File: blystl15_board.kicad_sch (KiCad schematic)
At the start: 3 parts, among them M1 BLYST NANO/L15

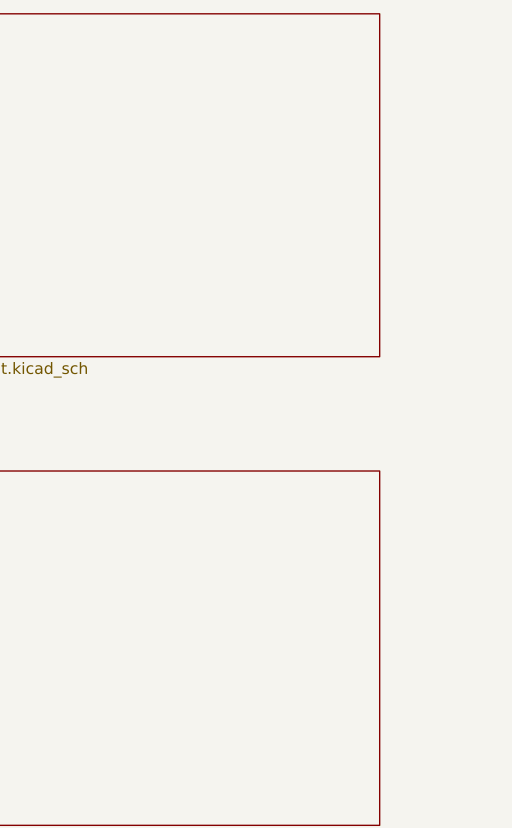
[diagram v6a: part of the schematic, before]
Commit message: PCB traces started
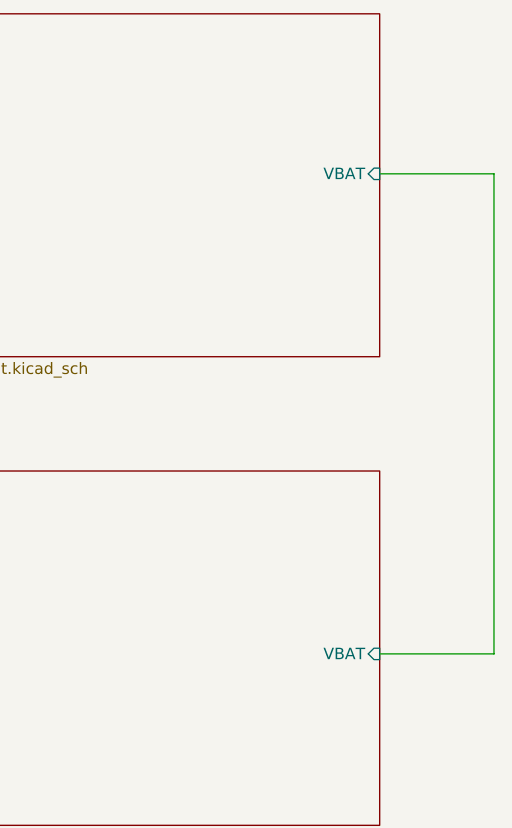
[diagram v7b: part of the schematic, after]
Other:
- sheet Power Management ports: added VBAT; removed none
- sheet Sensors ports: added VBAT; removed none
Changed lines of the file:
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@@
+	(wire
+		(pts
+			(xy 241.3 40.64) (xy 254 40.64)
+		)
+		(stroke
+			(width 0)
+			(type default)
+		)
+	)
 	(wire
 		(pts
@@
 	(wire
 		(pts
+			(xy 254 40.64) (xy 254 93.98)
+		)
+		(stroke
+			(width 0)
+			(type default)
+		)
+	)
+	(wire
+		(pts
 			(xy 158.75 138.43) (xy 177.8 138.43)
 		)
@@
 		(pts
 			(xy 158.75 100.33) (xy 177.8 100.33)
+		)
+		(stroke
+			(width 0)
+			(type default)
+		)
+	)
+	(wire
+		(pts
+			(xy 241.3 93.98) (xy 254 93.98)
 		)
 		(stroke
@@
 			)
 		)
+		(pin "VBAT" input
+			(at 241.3 93.98 0)
+			(effects
+				(font
+					(size 1.27 1.27)
+				)
+				(justify right)
+			)
+		)
 		(instances
 			(project "blystl15_board"
@@
 			)
 		)
+		(pin "VBAT" input
+			(at 241.3 40.64 0)
+			(effects
+				(font
+					(size 1.27 1.27)
+				)
+				(justify right)
+			)
+		)

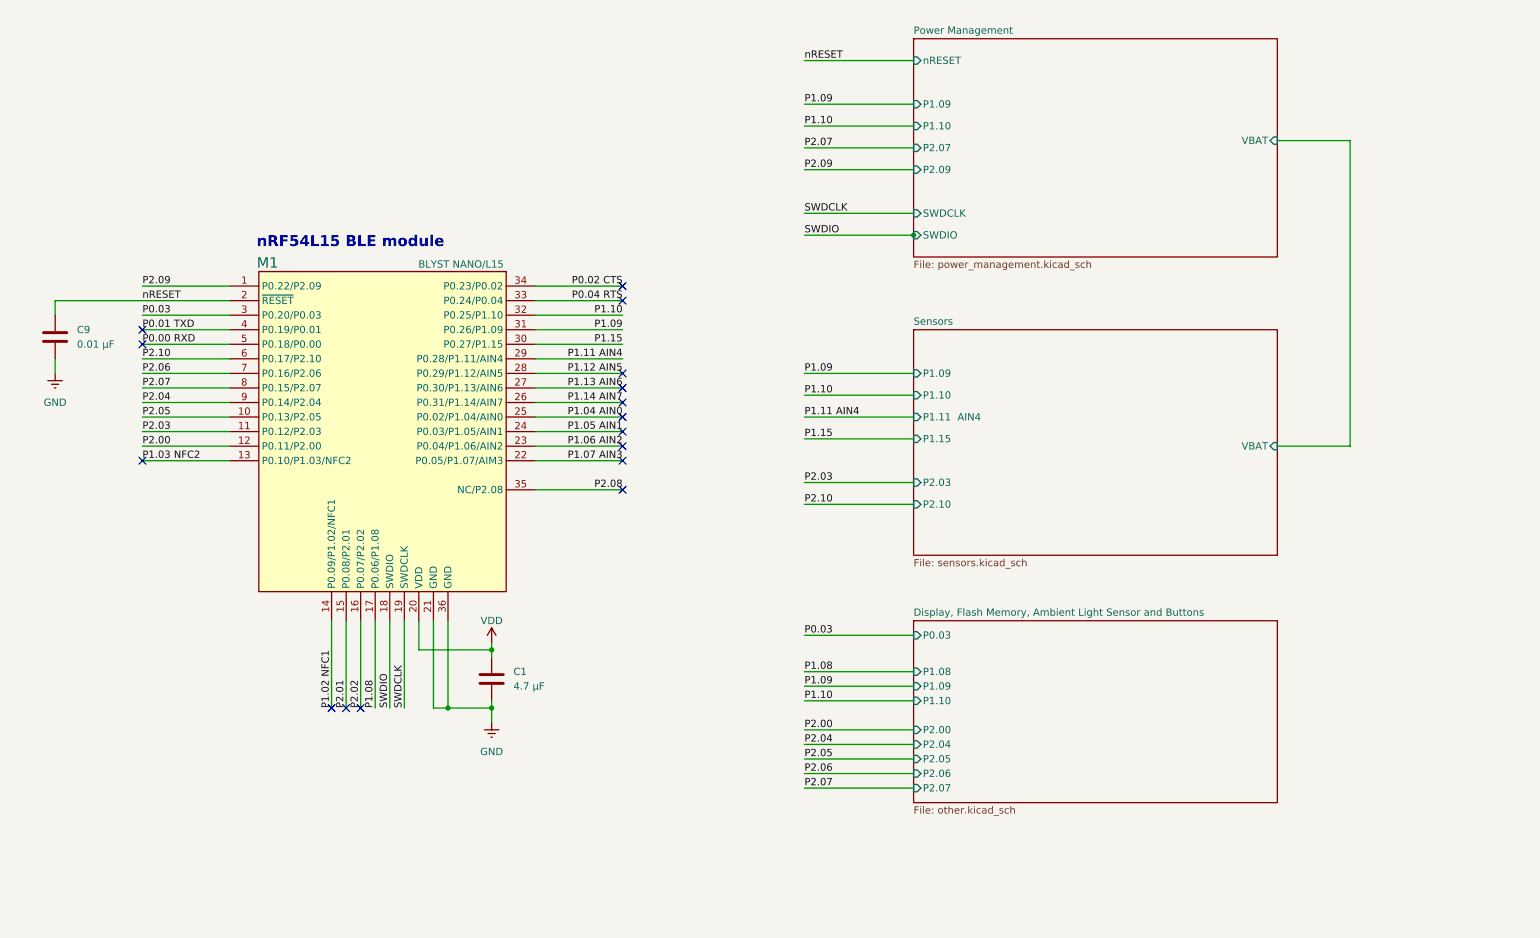
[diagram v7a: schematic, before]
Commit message: Full Redesign of the Watch PCB (DRC still not fully passed)
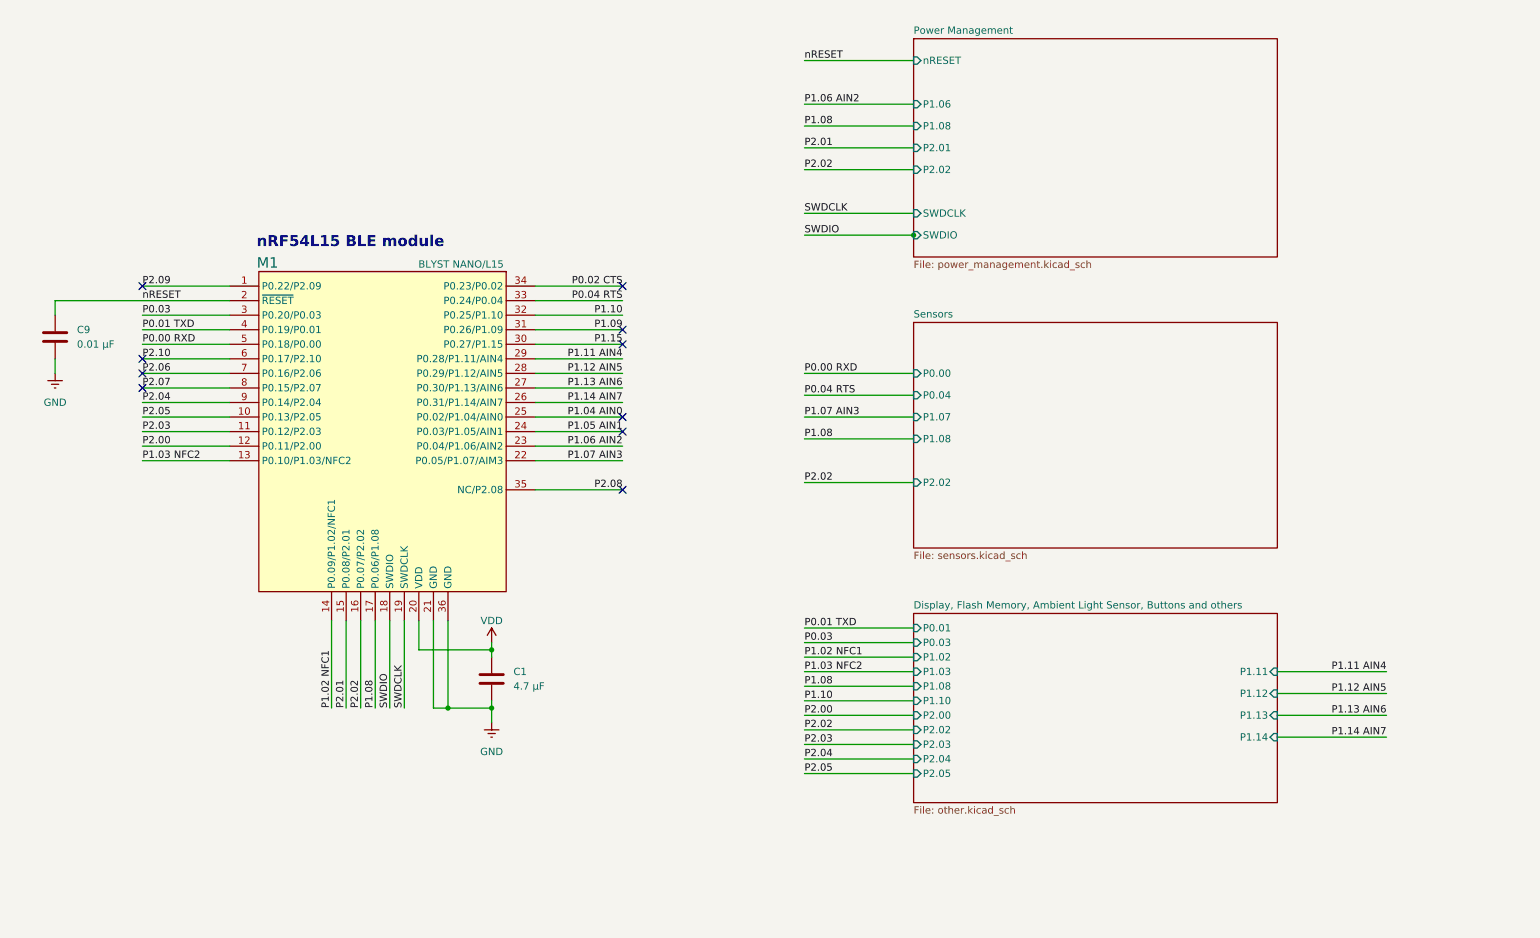
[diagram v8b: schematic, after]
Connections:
- no-connect marks 16 -> 10
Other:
- sheet Display, Flash Memory, Ambient Light Sensor and Buttons renamed Display, Flash Memory, Ambient Light Sensor, Buttons and others
- sheet Display, Flash Memory, Ambient Light Sensor, Buttons and others ports: added P0.01, P1.02, P1.03, P1.11, P1.12, P1.13, P1.14, P2.02, P2.03; removed P1.09, P2.06, P2.07
- sheet Power Management ports: added P1.06, P1.08, P2.01, P2.02; removed P1.09, P1.10, P2.07, P2.09, VBAT
- sheet Sensors ports: added P0.00, P0.04, P1.07, P1.08, P2.02; removed P1.09, P1.10, P1.11  AIN4, P1.15, P2.03, P2.10, VBAT
